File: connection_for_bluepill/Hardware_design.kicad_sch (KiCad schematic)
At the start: 1 part

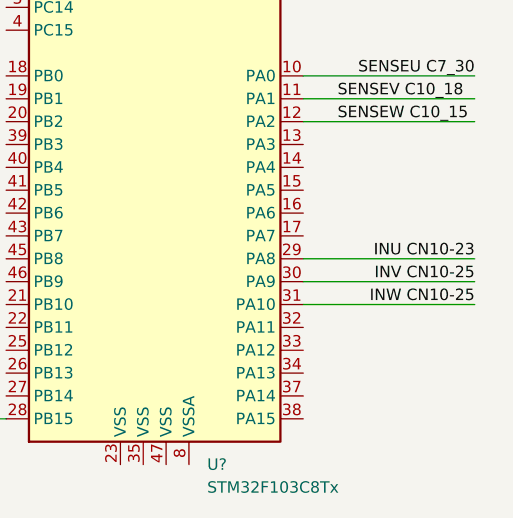
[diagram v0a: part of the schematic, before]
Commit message: fix bug in schematics
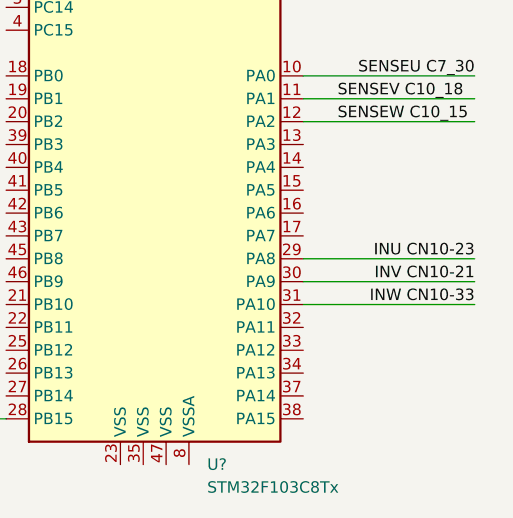
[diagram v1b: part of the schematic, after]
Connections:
- net INV  CN10-25 renamed INV  CN10-21
- net INW  CN10-25 renamed INW  CN10-33
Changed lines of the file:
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@@
     (effects (font (size 1.27 1.27)) (justify left bottom))
   )
-  (label "INV  CN10-25" (at 130.81 105.41 180)
+  (label "INV  CN10-21" (at 130.81 105.41 180)
     (effects (font (size 1.27 1.27)) (justify right bottom))
   )
@@
     (effects (font (size 1.27 1.27)) (justify left bottom))
   )
-  (label "INW  CN10-25" (at 130.81 107.95 180)
+  (label "INW  CN10-33" (at 130.81 107.95 180)
     (effects (font (size 1.27 1.27)) (justify right bottom))
   )
